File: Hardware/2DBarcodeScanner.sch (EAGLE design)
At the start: 33 parts, among them J1 BARCODE_ENGINE_CONN, Q1 600mA/40V, Q2 600mA/40V, U1 3.3V, U5 CH340C

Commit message: Version x02
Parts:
- removed C5: 0.1uF, SparkFun-Capacitors:0.1UF-0603-25V-(+80/-20%)
- removed C9: 10nF, SparkFun-Capacitors:10NF-0603-50V-10%
- removed H1, H4: STAND-OFF, SparkFun-Hardware:STAND-OFF
- removed J3: (no value), SparkFun-Connectors:CONN_05NO_SILK
- removed R12: 1k, SparkFun-Resistors:1KOHM-0603-1/10W-1%
- removed R4: 5.1k, SparkFun-Resistors:5.1KOHM5.1KOHM-0603-1/10W-1%
- removed U5: CH340C, SparkFun-IC-Comms:CH340C
- added JP1: JUMPER-SMT_2_NC_TRACE_SILK, SparkFun-Jumpers:JUMPER-SMT_2_NC_TRACE_SILK
- J4: device SparkFun-Connectors:USB_C2-LAYER -> SparkFun-Connectors:CONN_06NO_SILK_FEMALE_PTH
- R1: value 5.1k -> 470; device SparkFun-Resistors:5.1KOHM5.1KOHM-0603-1/10W-1% -> SparkFun-Resistors:470OHM-0603-1/10W-1%
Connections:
- removed net CC1: J4.CC1, R4.2
- removed net CC2: J4.CC2, R1.2
- removed net D+: J4.D+, U5.UD+
- removed net D-: J4.D-, U5.UD-
- removed net N$1: C9.1, U5.V3
- removed net N$6: D2.A, R12.1
- new net N$8: D2.A, JP1.1
- new net STATUS_OUT: J4.1, JP1.2, R1.1
- net 3.3V: now also J4.3; no longer J3.5, U5.VCC
- net 5V: no longer C5.1, J4.VBUS
- net GND: now also J4.6; no longer C5.2, C9.2, J3.2, J4.GND, R1.1, R4.1, U5.GND
- net N$4: now also R1.2; no longer R12.2
- net RXI: now also J4.5; no longer J3.3, U5.RXI
- net SCAN_TRIGGER: now also J4.2; no longer J3.1
- net SHLD: no longer J4.SHLD
- net TXO: now also J4.4; no longer J3.4, U5.TXO
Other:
- note removed: "USB to Serial"
- moved on the sheet: C1, C2, C3, D1, D2, J2, LS1, Q1, Q2, R10, R11, R2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

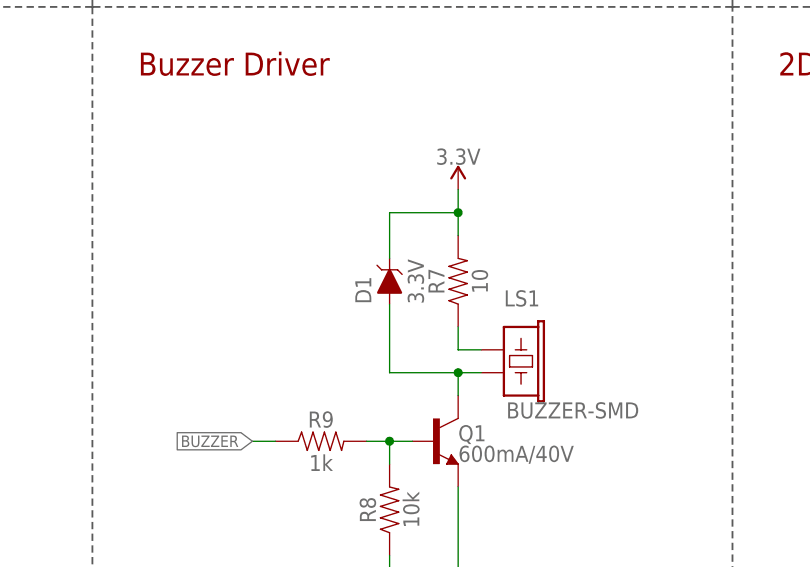
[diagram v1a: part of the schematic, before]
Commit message: Forgot to pull that stupid diode
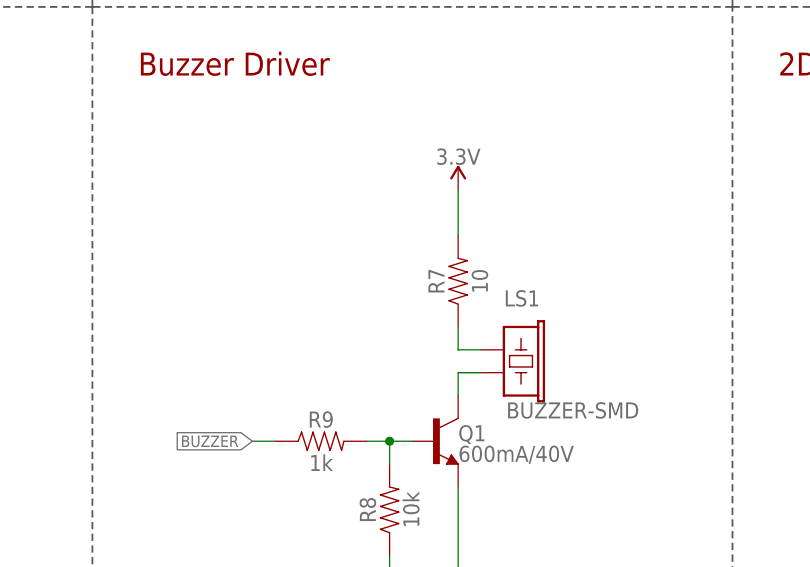
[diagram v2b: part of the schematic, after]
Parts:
- removed D1: 3.3V, SparkFun-DiscreteSemi:DIODE-ZENER-MM3Z3V3T1G
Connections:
- net 3.3V: no longer D1.C
- net N$2: no longer D1.A
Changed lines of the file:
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@@
 <part name="Q1" library="SparkFun-DiscreteSemi" deviceset="TRANS_NPN" device="-MMBT2222AL" value="600mA/40V"/>
 <part name="LS1" library="SparkFun-Electromechanical" deviceset="BUZZER" device="-SMD"/>
-<part name="D1" library="SparkFun-DiscreteSemi" deviceset="DIODE-ZENER" device="-MM3Z3V3T1G" value="3.3V"/>
 <part name="R7" library="SparkFun-Resistors" deviceset="10OHM" device="-0603-1/10W-5%" value="10"/>
 <part name="R8" library="SparkFun-Resistors" deviceset="10KOHM" device="-0603-1/10W-1%" value="10k"/>
@@
 <attribute name="VALUE" x="122.174" y="76.2" size="1.778" layer="96" font="vector"/>
 </instance>
-<instance part="D1" gate="G$1" x="109.22" y="91.44" smashed="yes" rot="R90">
-<attribute name="NAME" x="107.188" y="88.9" size="1.778" layer="95" font="vector" rot="R90"/>
-<attribute name="VALUE" x="111.252" y="88.9" size="1.778" layer="96" font="vector" rot="R90" align="top-left"/>
-</instance>
 <instance part="R7" gate="G$1" x="116.84" y="91.44" smashed="yes" rot="R90">
 <attribute name="NAME" x="115.316" y="91.44" size="1.778" layer="95" font="vector" rot="R90" align="bottom-center"/>
@@
 </segment>
 <segment>
-<pinref part="D1" gate="G$1" pin="C"/>
-<wire x1="109.22" y1="93.98" x2="109.22" y2="99.06" width="0.1524" layer="91"/>
-<wire x1="109.22" y1="99.06" x2="116.84" y2="99.06" width="0.1524" layer="91"/>
 <pinref part="R7" gate="G$1" pin="2"/>
-<wire x1="116.84" y1="99.06" x2="116.84" y2="96.52" width="0.1524" layer="91"/>
-<wire x1="116.84" y1="99.06" x2="116.84" y2="101.6" width="0.1524" layer="91"/>
-<junction x="116.84" y="99.06"/>
+<wire x1="116.84" y1="96.52" x2="116.84" y2="101.6" width="0.1524" layer="91"/>
 <pinref part="SUPPLY5" gate="G$1" pin="3.3V"/>
 </segment>
@@
 <wire x1="116.84" y1="78.74" x2="116.84" y2="81.28" width="0.1524" layer="91"/>
 <wire x1="116.84" y1="81.28" x2="119.38" y2="81.28" width="0.1524" layer="91"/>
-<wire x1="116.84" y1="81.28" x2="109.22" y2="81.28" width="0.1524" layer="91"/>
-<junction x="116.84" y="81.28"/>
-<pinref part="D1" gate="G$1" pin="A"/>
-<wire x1="109.22" y1="88.9" x2="109.22" y2="81.28" width="0.1524" layer="91"/>
-</segment>
-</net>
+</segment>
+</net>
